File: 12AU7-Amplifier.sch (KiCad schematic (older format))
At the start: 29 parts, among them CON1 AudioIn, CON2 AudioOut, J1 Barrel_Jack, Q1 IRF510, Q2 IRF510, SW1 SW_SPDT, U1 12AU7, U2 LM317, U3 LM317

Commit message: Redo schematic and update .gitignore
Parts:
- removed CON1: AudioIn, digikey-footprints:Headphone_Jack_3.5mm_SJ1-3523N, symbol dk_Barrel-Audio-Connectors:SJ1-3523N
- removed CON2: AudioOut, digikey-footprints:Headphone_Jack_3.5mm_SJ1-3523N, symbol dk_Barrel-Audio-Connectors:SJ1-3523N
- removed U1: 12AU7, 12AU7:12AU7, symbol Valve:ECC81
- added J? (x2): AudioJack3, symbol Connector:AudioJack3
- added U? (x3): 12AU7, Valve:Valve_Noval_P, symbol Valve:ECC81
- renumbered C2 to C?, C4 to C?, C6 to C?, C7 to C?, C3 to C?, C1 to C?, C5 to C?, D1 to D?, J1 to J?, Q2 to Q?, Q1 to Q?, R5 to R?, R2 to R?, R7 to R?, R9 to R?, R1 to R?, R4 to R?, R8 to R?, R6 to R?, R3 to R?, RV1 to RV?, RV3 to RV?, RV2 to RV?, SW1 to SW?, U3 to U?, U2 to U?
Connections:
- wire segments 128 -> 117
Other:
- moved on the sheet: C?, Q?, R?, RV?, U?

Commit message: Updated page settings
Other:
- moved on the sheet: C?, D?, J?, Q?, R?, RV?, SW?, U?, U?A, U?B, U?C

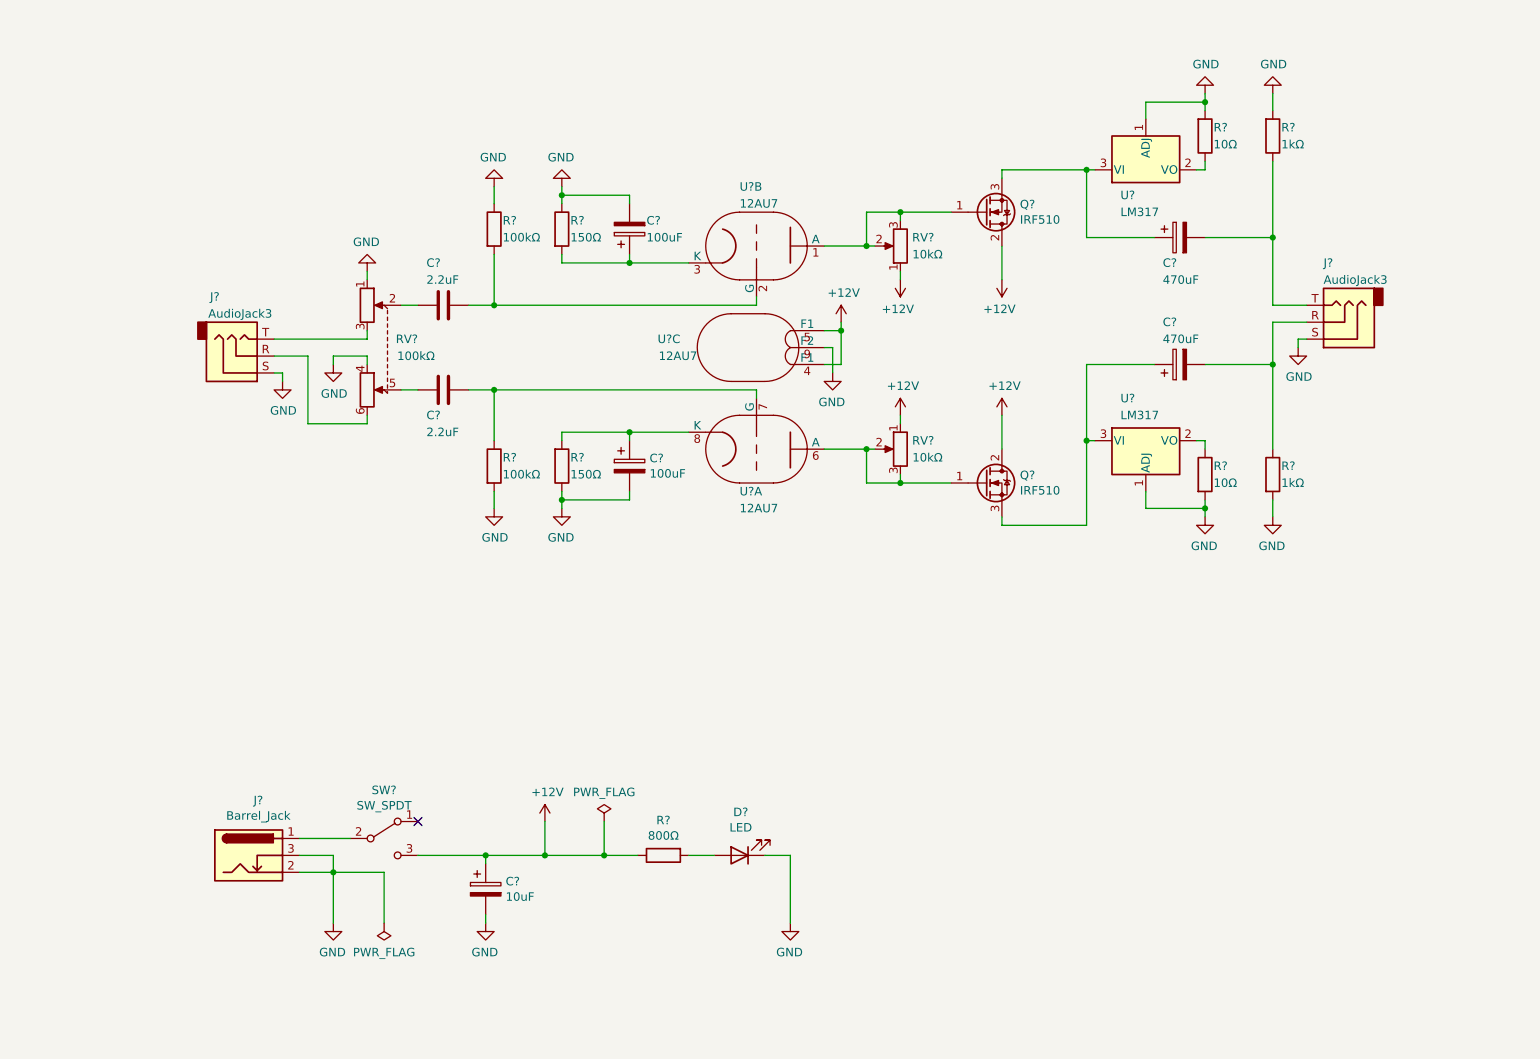
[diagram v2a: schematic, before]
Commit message: Reorganize symbol/footprint libraries, add audio jack
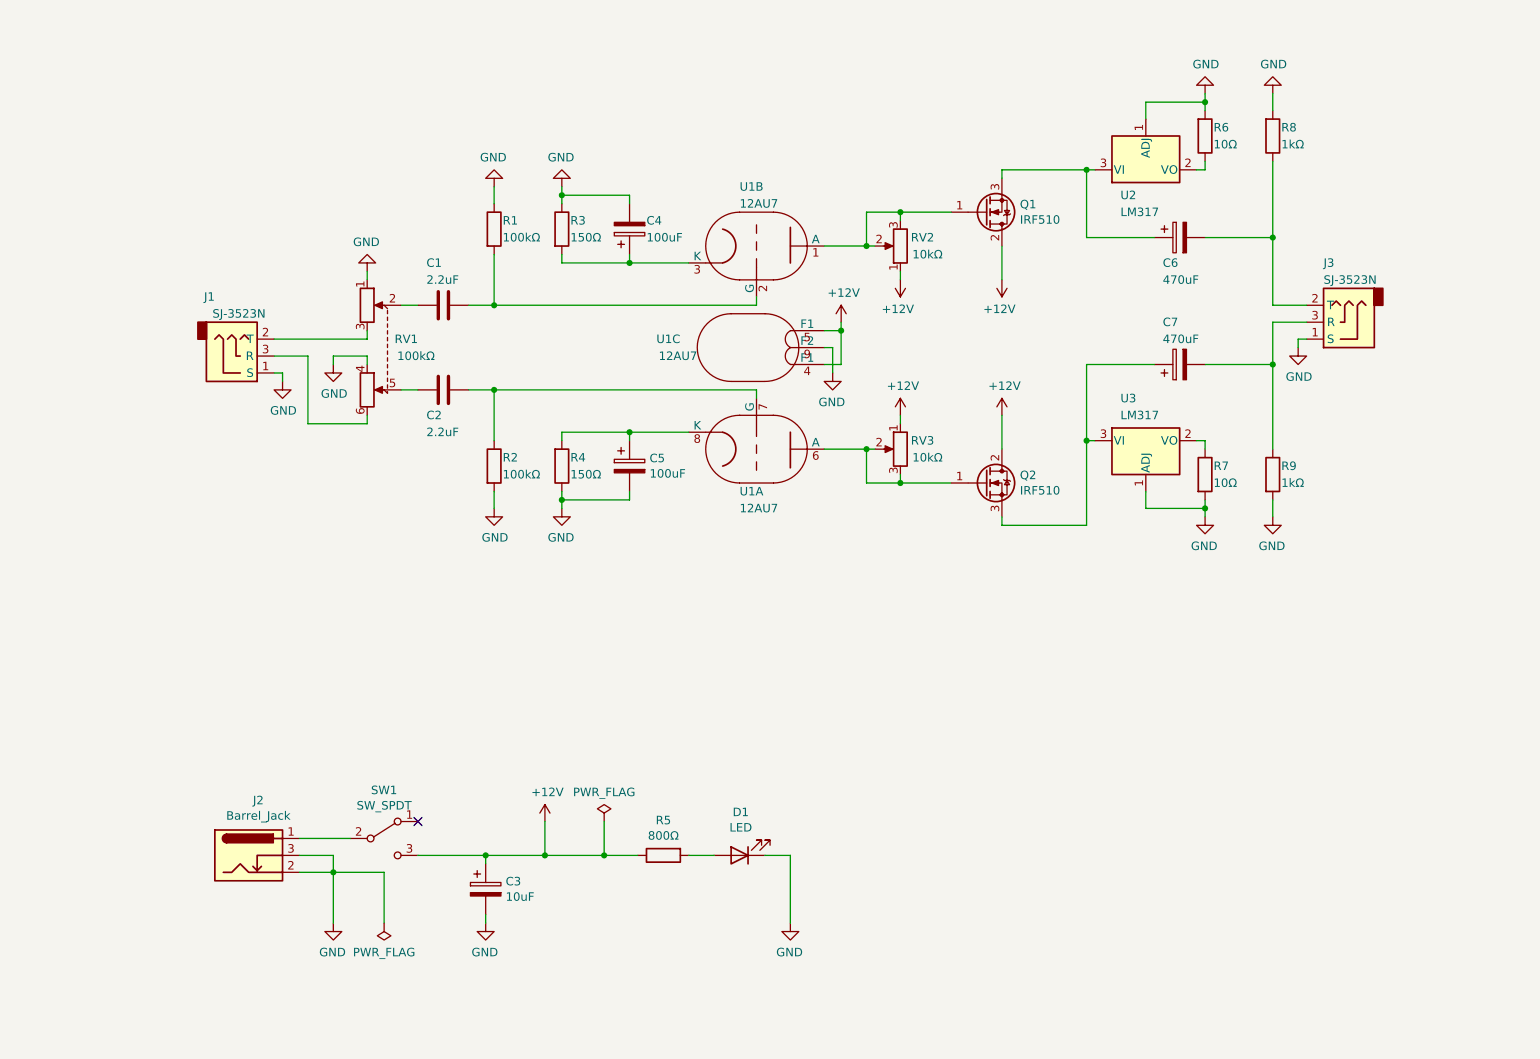
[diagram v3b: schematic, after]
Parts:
- removed J? (x2): AudioJack3, symbol Connector:AudioJack3
- added J1, J3: SJ-3523N, symbol 12AU7-Amplifier:SJ-3523N
- RV1: renamed from RV?; footprint Alps_100KAX2:Alps_100KAX2 -> 12AU7-Amplifier:Alps_100KAX2
- SW1: renamed from SW?; footprint Switch_200MSP1T1B2M6QE:Switch_SPDT -> 12AU7-Amplifier:Switch_SPDT
- U1: renamed from U?; footprint Valve:Valve_Noval_P -> 12AU7-Amplifier:12AU7
- gave numbers to parts that had none: 24
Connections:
- net GND: now also J1.1 (S), J3.1 (S)
- net at RV1.3: now also J1.2 (T)
- net at RV1.6: now also J1.3 (R)
- net at C7.2, R9.1: now also J3.3 (R)
- net at C6.2, R8.1: now also J3.2 (T)

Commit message: Added components for layout, added 3D models
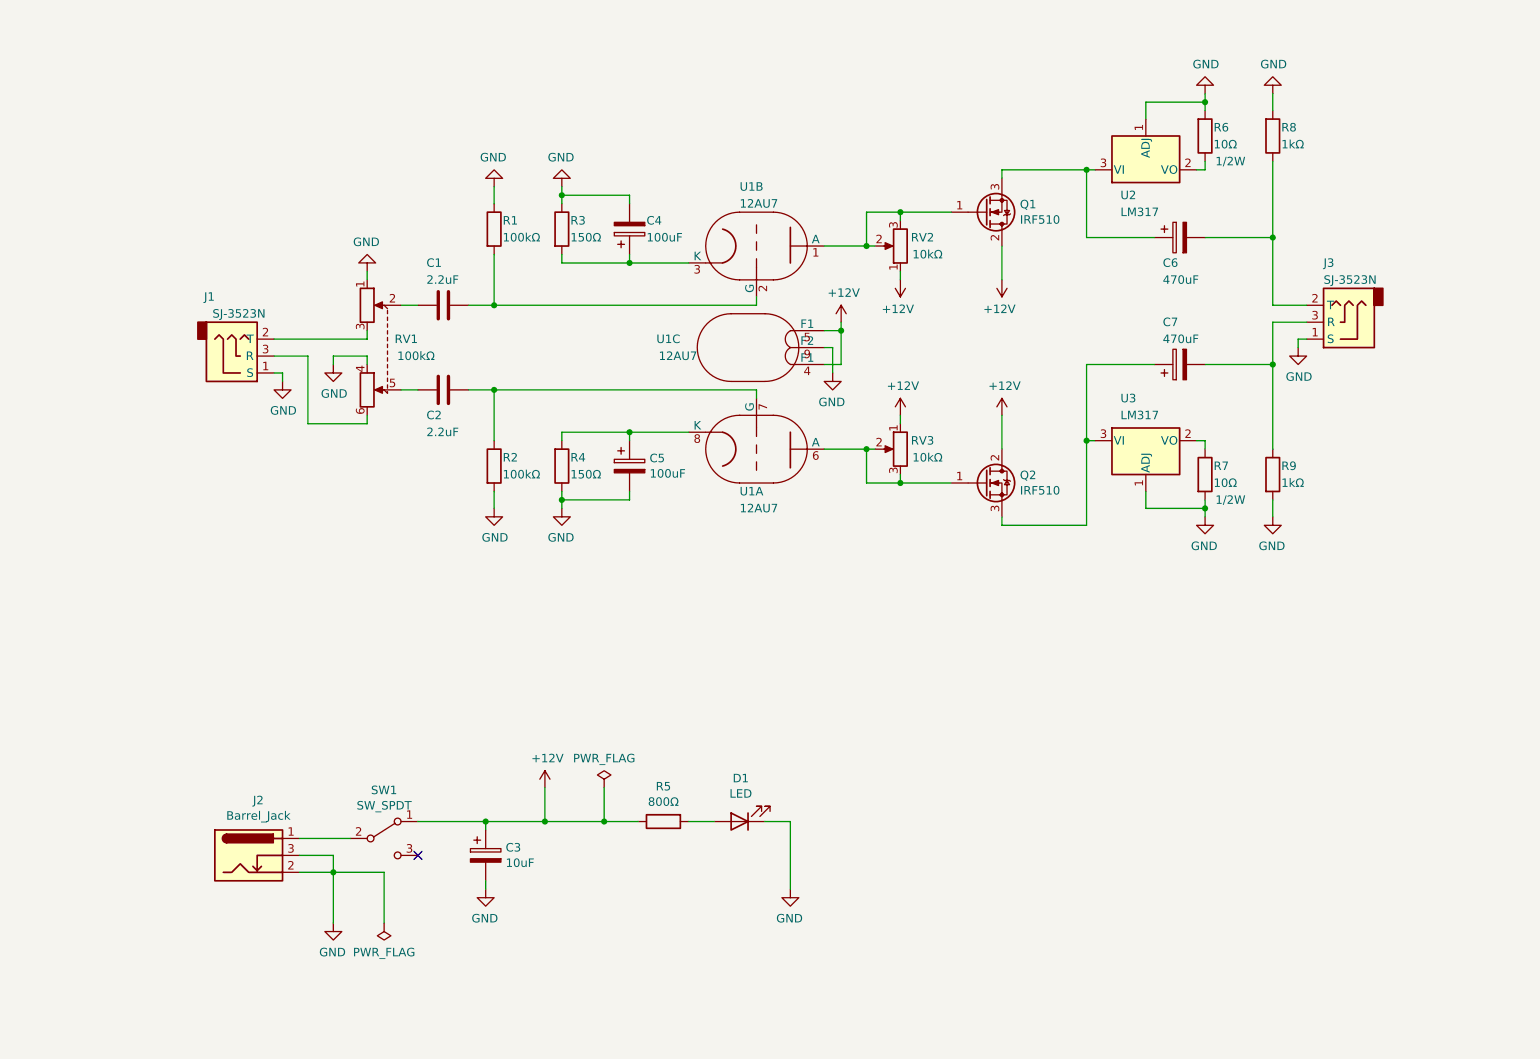
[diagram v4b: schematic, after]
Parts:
- J1, J3: footprint (none) -> 12AU7-Amplifier:Headphone_Jack_3.5mm_SJ1-3523N
- J2: footprint Connector_BarrelJack:BarrelJack_Horizontal -> 12AU7-Amplifier:BarrelJack_Horizontal
- R6, R7: Field4 (none) -> 1/2W
- SW1: footprint 12AU7-Amplifier:Switch_SPDT -> 12AU7-Amplifier:100SP1T2B4M7QE
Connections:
- net +12V: now also SW1.1 (A); no longer SW1.3 (C)
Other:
- moved on the sheet: C3, D1, R5
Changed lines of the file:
@@
 F 2 "Resistor_THT:R_Axial_DIN0207_L6.3mm_D2.5mm_P10.16mm_Horizontal" V 7930 1950 50  0001 C CNN
 F 3 "~" H 8000 1950 50  0001 C CNN
+F 4 "1/2W" H 8150 2100 50  0000 C CNN "Field4"
 	1    8000 1950
 	1    0    0    1
@@
 F 2 "Resistor_THT:R_Axial_DIN0207_L6.3mm_D2.5mm_P10.16mm_Horizontal" V 7930 3950 50  0001 C CNN
 F 3 "~" H 8000 3950 50  0001 C CNN
+F 4 "1/2W" H 8150 3800 50  0000 C CNN "Field4"
 	1    8000 3950
 	1    0    0    -1
@@
 $EndComp
 $Comp
-L Connector:Barrel_Jack_Switch J2
-U 1 1 5CC919F9
-P 2350 6200
-F 0 "J2" H 2407 6525 50  0000 C CNN
-F 1 "Barrel_Jack" H 2407 6434 50  0000 C CNN
-F 2 "Connector_BarrelJack:BarrelJack_Horizontal" H 2400 6160 50  0001 C CNN
-F 3 "~" H 2400 6160 50  0001 C CNN
-	1    2350 6200
-	1    0    0    -1
-$EndComp
+L 12AU7-Amplifier:SJ-3523N J3
+U 1 1 5FAD58EC
+P 8800 3050
+F 0 "J3" H 8900 2700 50  0000 R CNN
+F 1 "SJ-3523N" H 8900 2800 50  0000 R CNN
+F 2 "12AU7-Amplifier:Headphone_Jack_3.5mm_SJ1-3523N" H 8800 3050 50  0001 C CNN
+F 3 "https://www.cuidevices.com/product/resource/sj1-352xn.pdf" H 8800 3050 50  0001 C CNN
+	1    8800 3050
+	-1   0    0    1
+$EndComp
+Wire Wire Line
+	2500 3250 2700 3250
+Wire Wire Line
+	2500 3150 3050 3150
+Wire Wire Line
+	2500 3350 2550 3350
+$Comp
+L 12AU7-Amplifier:SJ-3523N J1
+U 1 1 5FAD47CB
+P 2300 3250
+F 0 "J1" H 2150 2900 50  0000 R CNN
+F 1 "SJ-3523N" H 2450 3000 50  0000 R CNN
+F 2 "12AU7-Amplifier:Headphone_Jack_3.5mm_SJ1-3523N" H 2300 3250 50  0001 C CNN
+F 3 "https://www.cuidevices.com/product/resource/sj1-352xn.pdf" H 2300 3250 50  0001 C CNN
+	1    2300 3250
+	1    0    0    1
+$EndComp
+$Comp
+L power:+12V #PWR08
+U 1 1 5CCB4117
+P 4100 5800
+F 0 "#PWR08" H 4100 5650 50  0001 C CNN
+F 1 "+12V" H 4115 5973 50  0000 C CNN
+F 2 "" H 4100 5800 50  0001 C CNN
+F 3 "" H 4100 5800 50  0001 C CNN
+	1    4100 5800
+	1    0    0    -1
+$EndComp
+Wire Wire Line
+	4100 5800 4100 6000
+$Comp
+L power:PWR_FLAG #FLG02
+U 1 1 5CD1CF3B
+P 4450 5800
+F 0 "#FLG02" H 4450 5875 50  0001 C CNN
+F 1 "PWR_FLAG" H 4450 5973 50  0000 C CNN
+F 2 "" H 4450 5800 50  0001 C CNN
+F 3 "~" H 4450 5800 50  0001 C CNN
+	1    4450 5800
+	1    0    0    -1
+$EndComp
+Wire Wire Line
+	4450 5800 4450 6000
+$Comp
+L power:PWR_FLAG #FLG01
+U 1 1 5CD351E6
+P 3150 6600
+F 0 "#FLG01" H 3150 6675 50  0001 C CNN
+F 1 "PWR_FLAG" H 3150 6773 50  0000 C CNN
+F 2 "" H 3150 6600 50  0001 C CNN
+F 3 "~" H 3150 6600 50  0001 C CNN
+	1    3150 6600
+	-1   0    0    1
+$EndComp
+Wire Wire Line
+	3150 6600 3150 6300
+Wire Wire Line
+	3350 6000 3750 6000
+NoConn ~ 3350 6200
+$Comp
+L Switch:SW_SPDT SW1
+U 1 1 5CB5A4D3
+P 3150 6100
+F 0 "SW1" H 3150 6385 50  0000 C CNN
+F 1 "SW_SPDT" H 3150 6294 50  0000 C CNN
+F 2 "12AU7-Amplifier:100SP1T2B4M7QE" H 3150 6100 50  0001 C CNN
+F 3 "~" H 3150 6100 50  0001 C CNN
+	1    3150 6100
+	1    0    0    -1
+$EndComp
+Wire Wire Line
+	3750 6400 3750 6350
+$Comp
+L power:GND #PWR05
+U 1 1 5CB85CDE
+P 3750 6400
+F 0 "#PWR05" H 3750 6150 50  0001 C CNN
+F 1 "GND" H 3755 6227 50  0000 C CNN
+F 2 "" H 3750 6400 50  0001 C CNN
+F 3 "" H 3750 6400 50  0001 C CNN
+	1    3750 6400
+	-1   0    0    -1
+$EndComp
+Connection ~ 3750 6000
+Wire Wire Line
+	3750 6050 3750 6000
+$Comp
+L Device:CP C3
+U 1 1 5CB59ACC
+P 3750 6200
+F 0 "C3" H 3868 6246 50  0000 L CNN
+F 1 "10uF" H 3868 6155 50  0000 L CNN
+F 2 "Capacitor_THT:CP_Radial_D5.0mm_P2.50mm" H 3788 6050 50  0001 C CNN
+F 3 "~" H 3750 6200 50  0001 C CNN
+	1    3750 6200
+	1    0    0    -1
+$EndComp
+Wire Wire Line
+	4100 6000 3750 6000
+Wire Wire Line
+	2850 6200 2850 6300
+Wire Wire Line
+	2650 6200 2850 6200
+Connection ~ 4450 6000
+Connection ~ 4100 6000
+Wire Wire Line
+	4100 6000 4450 6000
+Connection ~ 2850 6300
+Wire Wire Line
+	3150 6300 2850 6300
+Wire Wire Line
+	5550 6000 5550 6400
+Wire Wire Line
+	5400 6000 5550 6000
+$Comp
+L power:GND #PWR011
+U 1 1 5CCC0B1A
+P 5550 6400
+F 0 "#PWR011" H 5550 6150 50  0001 C CNN
+F 1 "GND" H 5555 6227 50  0000 C CNN
+F 2 "" H 5550 6400 50  0001 C CNN
+F 3 "" H 5550 6400 50  0001 C CNN
+	1    5550 6400
+	-1   0    0    -1
+$EndComp
+Wire Wire Line
+	4950 6000 5100 6000
+$Comp
+L Device:LED D1
+U 1 1 5CCBBC9F
+P 5250 6000
+F 0 "D1" H 5243 5745 50  0000 C CNN
+F 1 "LED" H 5243 5836 50  0000 C CNN
+F 2 "LED_THT:LED_D5.0mm_Horizontal_O1.27mm_Z3.0mm" H 5250 6000 50  0001 C CNN
+F 3 "~" H 5250 6000 50  0001 C CNN
+	1    5250 6000
+	-1   0    0    1
+$EndComp
+Wire Wire Line
+	4450 6000 4650 6000
+$Comp
+L Device:R R5
+U 1 1 5CC9A575
+P 4800 6000
+F 0 "R5" V 4593 6000 50  0000 C CNN
+F 1 "800Ω" V 4684 6000 50  0000 C CNN
+F 2 "Resistor_THT:R_Axial_DIN0207_L6.3mm_D2.5mm_P10.16mm_Horizontal" V 4730 6000 50  0001 C CNN
+F 3 "~" H 4800 6000 50  0001 C CNN
+	1    4800 6000
+	0    -1   1    0
+$EndComp
+Wire Wire Line
+	2650 6100 2950 6100
+Wire Wire Line
+	2850 6300 2650 6300
+Wire Wire Line
+	2850 6600 2850 6300
 $Comp
 L power:GND #PWR03
@@
 	-1   0    0    -1
 $EndComp
-Wire Wire Line
-	2850 6600 2850 6300
-Wire Wire Line
-	2850 6300 2650 6300
-Wire Wire Line
-	2650 6100 2950 6100
-$Comp
-L Device:R R5
-U 1 1 5CC9A575
-P 4800 6200
-F 0 "R5" V 4593 6200 50  0000 C CNN
-F 1 "800Ω" V 4684 6200 50  0000 C CNN
-F 2 "Resistor_THT:R_Axial_DIN0207_L6.3mm_D2.5mm_P10.16mm_Horizontal" V 4730 6200 50  0001 C CNN
-F 3 "~" H 4800 6200 50  0001 C CNN
-	1    4800 6200
-	0    -1   1    0
-$EndComp
-Wire Wire Line
-	4450 6200 4650 6200
-$Comp
-L Device:LED D1
-U 1 1 5CCBBC9F
-P 5250 6200
-F 0 "D1" H 5243 5945 50  0000 C CNN
-F 1 "LED" H 5243 6036 50  0000 C CNN
-F 2 "LED_THT:LED_D5.0mm_Horizontal_O1.27mm_Z3.0mm" H 5250 6200 50  0001 C CNN
-F 3 "~" H 5250 6200 50  0001 C CNN
-	1    5250 6200
-	-1   0    0    1
-$EndComp
-Wire Wire Line
-	4950 6200 5100 6200
-$Comp
-L power:GND #PWR011
-U 1 1 5CCC0B1A
-P 5550 6600
-F 0 "#PWR011" H 5550 6350 50  0001 C CNN
-F 1 "GND" H 5555 6427 50  0000 C CNN
-F 2 "" H 5550 6600 50  0001 C CNN
-F 3 "" H 5550 6600 50  0001 C CNN
-	1    5550 6600
-	-1   0    0    -1
-$EndComp
-Wire Wire Line
-	5400 6200 5550 6200
-Wire Wire Line
-	5550 6200 5550 6600
-Wire Wire Line
-	3150 6300 2850 6300
-Connection ~ 2850 6300
-Wire Wire Line
-	4100 6200 4450 6200
-Connection ~ 4100 6200
-Connection ~ 4450 6200
-Wire Wire Line
-	2650 6200 2850 6200
-Wire Wire Line
-	2850 6200 2850 6300
-Wire Wire Line
-	4100 6200 3750 6200
-$Comp
-L Device:CP C3
-U 1 1 5CB59ACC
-P 3750 6400
-F 0 "C3" H 3868 6446 50  0000 L CNN
-F 1 "10uF" H 3868 6355 50  0000 L CNN
-F 2 "Capacitor_THT:CP_Radial_D5.0mm_P2.50mm" H 3788 6250 50  0001 C CNN
-F 3 "~" H 3750 6400 50  0001 C CNN
-	1    3750 6400
-	1    0    0    -1
-$EndComp
-Wire Wire Line
-	3750 6250 3750 6200
-Connection ~ 3750 6200
-$Comp
-L power:GND #PWR05
-U 1 1 5CB85CDE
-P 3750 6600
-F 0 "#PWR05" H 3750 6350 50  0001 C CNN
-F 1 "GND" H 3755 6427 50  0000 C CNN
-F 2 "" H 3750 6600 50  0001 C CNN
-F 3 "" H 3750 6600 50  0001 C CNN
-	1    3750 6600
-	-1   0    0    -1
-$EndComp
-Wire Wire Line
-	3750 6600 3750 6550
-$Comp
-L Switch:SW_SPDT SW1
-U 1 1 5CB5A4D3
-P 3150 6100
-F 0 "SW1" H 3150 6385 50  0000 C CNN
-F 1 "SW_SPDT" H 3150 6294 50  0000 C CNN
-F 2 "12AU7-Amplifier:Switch_SPDT" H 3150 6100 50  0001 C CNN
-F 3 "~" H 3150 6100 50  0001 C CNN
-	1    3150 6100
-	1    0    0    -1
-$EndComp
-NoConn ~ 3350 6000
-Wire Wire Line
-	3350 6200 3750 6200
-Wire Wire Line
-	3150 6600 3150 6300
-$Comp
-L power:PWR_FLAG #FLG01
-U 1 1 5CD351E6
-P 3150 6600
-F 0 "#FLG01" H 3150 6675 50  0001 C CNN
-F 1 "PWR_FLAG" H 3150 6773 50  0000 C CNN
-F 2 "" H 3150 6600 50  0001 C CNN
-F 3 "~" H 3150 6600 50  0001 C CNN
-	1    3150 6600
-	-1   0    0    1
-$EndComp
-Wire Wire Line
-	4450 6000 4450 6200
-$Comp
-L power:PWR_FLAG #FLG02
-U 1 1 5CD1CF3B
-P 4450 6000
-F 0 "#FLG02" H 4450 6075 50  0001 C CNN
-F 1 "PWR_FLAG" H 4450 6173 50  0000 C CNN
-F 2 "" H 4450 6000 50  0001 C CNN
-F 3 "~" H 4450 6000 50  0001 C CNN
-	1    4450 6000
-	1    0    0    -1
-$EndComp
-Wire Wire Line
-	4100 6000 4100 6200
-$Comp
-L power:+12V #PWR08
-U 1 1 5CCB4117
-P 4100 6000
-F 0 "#PWR08" H 4100 5850 50  0001 C CNN
-F 1 "+12V" H 4115 6173 50  0000 C CNN
-F 2 "" H 4100 6000 50  0001 C CNN
-F 3 "" H 4100 6000 50  0001 C CNN
-	1    4100 6000
-	1    0    0    -1
-$EndComp
-$Comp
-L 12AU7-Amplifier:SJ-3523N J3
-U 1 1 5FAD58EC
-P 8800 3050
-F 0 "J3" H 8900 2700 50  0000 R CNN
-F 1 "SJ-3523N" H 8900 2800 50  0000 R CNN
-F 2 "" H 8800 3050 50  0001 C CNN
-F 3 "https://www.cuidevices.com/product/resource/sj1-352xn.pdf" H 8800 3050 50  0001 C CNN
-	1    8800 3050
-	-1   0    0    1
-$EndComp
-Wire Wire Line
-	2500 3250 2700 3250
-Wire Wire Line
-	2500 3150 3050 3150
-Wire Wire Line
-	2500 3350 2550 3350
-$Comp
-L 12AU7-Amplifier:SJ-3523N J1
-U 1 1 5FAD47CB
-P 2300 3250
-F 0 "J1" H 2150 2900 50  0000 R CNN
-F 1 "SJ-3523N" H 2450 3000 50  0000 R CNN
-F 2 "" H 2300 3250 50  0001 C CNN
-F 3 "https://www.cuidevices.com/product/resource/sj1-352xn.pdf" H 2300 3250 50  0001 C CNN
-	1    2300 3250
-	1    0    0    1
+$Comp
+L Connector:Barrel_Jack_Switch J2
+U 1 1 5CC919F9
+P 2350 6200
+F 0 "J2" H 2407 6525 50  0000 C CNN
+F 1 "Barrel_Jack" H 2407 6434 50  0000 C CNN
+F 2 "12AU7-Amplifier:BarrelJack_Horizontal" H 2400 6160 50  0001 C CNN
+F 3 "~" H 2400 6160 50  0001 C CNN
+	1    2350 6200
+	1    0    0    -1
 $EndComp
 $EndSCHEMATC
